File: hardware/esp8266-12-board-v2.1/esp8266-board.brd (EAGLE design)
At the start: 35.4 x 38 mm, 26 parts, among them T1 AMS1117, T2 LM7805

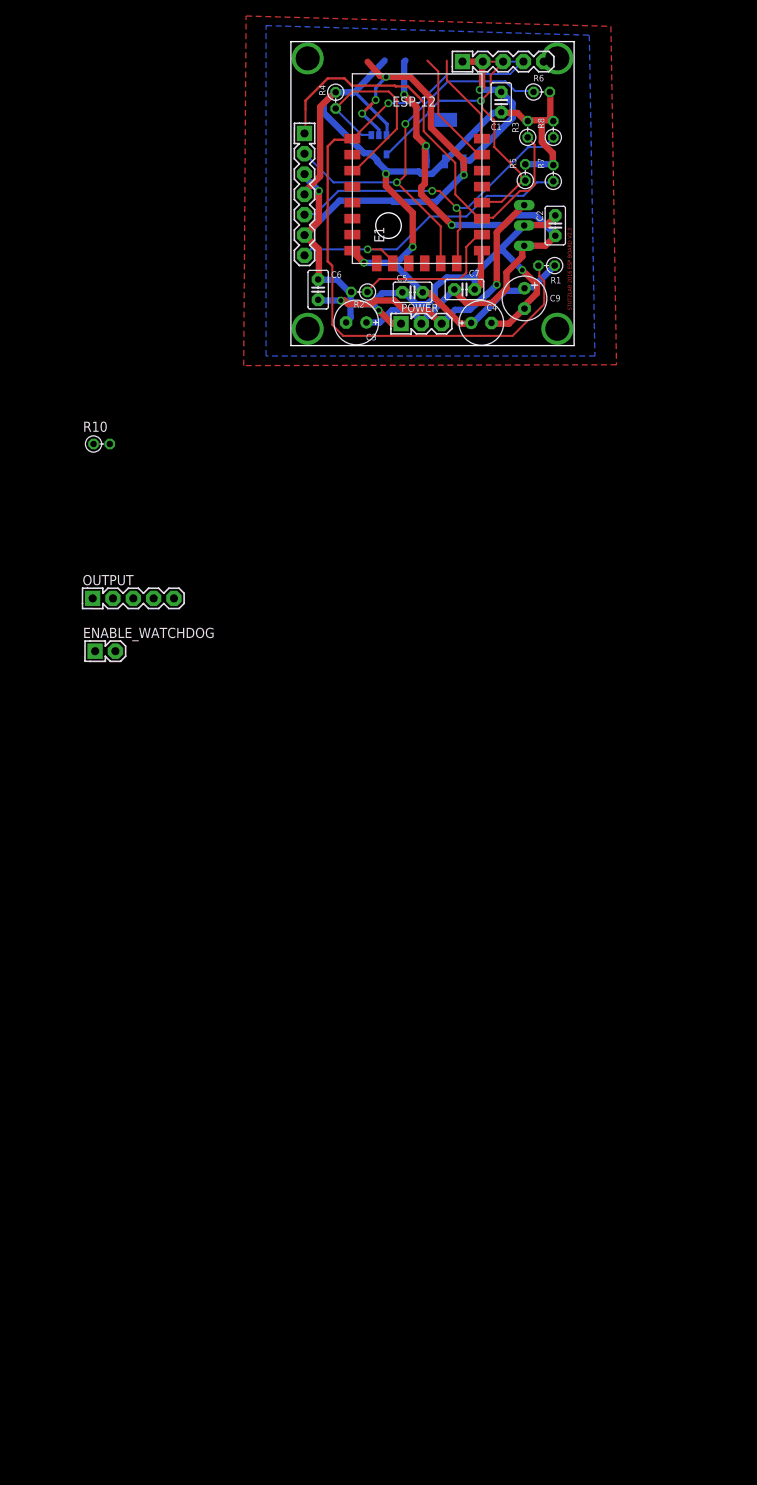
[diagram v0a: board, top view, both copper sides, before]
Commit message: Added watchdog from maxim
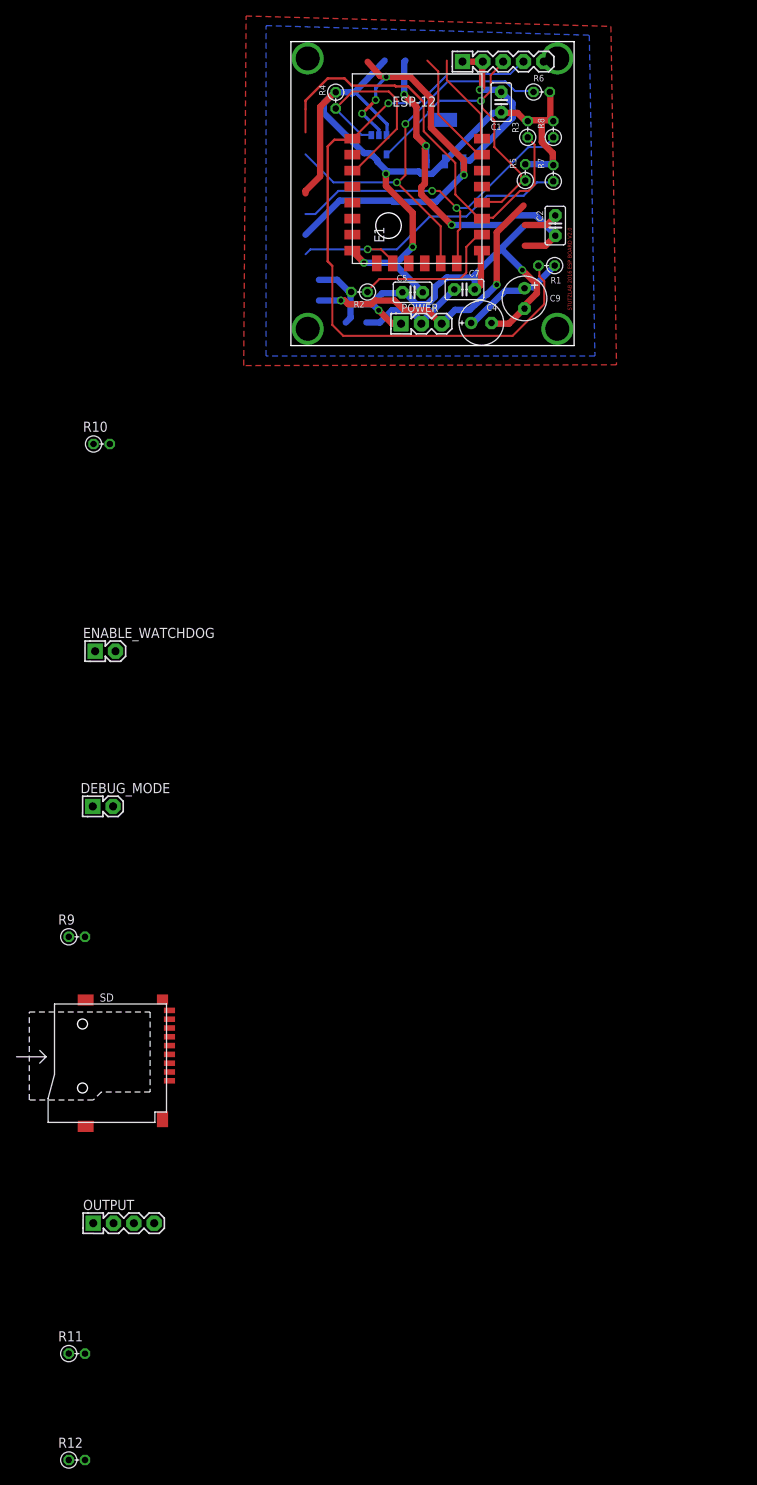
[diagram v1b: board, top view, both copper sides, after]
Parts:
- removed C3: 470uF, rcl:E2,5-6E
- removed C6: 0.22uF, capacitor-wima:C2.5-2
- removed SD1: CS SI GND 3.3V SCK GND SO, stutz-eagle:PIN-HEADER-7PIN
- removed T2: LM7805, stutz-components-library:TO-220
- added DEBUG_MODE: PIN-HEADER-2PIN, stutz-components-library:PIN-HEADER-2PIN
- added R11, R12: 500, stutz-components-library:RESISTOR-V1
- added R9: 10k, stutz-components-library:RESISTOR-V1
- added SD: MICROSD-TRANSFLASH, stutz-components-library:MICROSD-TRANSFLASH
- OUTPUT: value PIN-HEADER-5PIN -> PIN-HEADER-4PIN; device stutz-components-library:PIN-HEADER-5PIN -> stutz-components-library:PIN-HEADER-4PIN
- POWER: value GND +5V <35V -> GND +5V +3.3V
- W1: value TPS3823-33 -> MAX6373KA+T
- moved OUTPUT 78.1 mm to (-20.9, -109.7)
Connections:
- removed net +24V: C6.1, POWER.3, T2.INPUT
- new net N$6: C5.2
- new net N$7: FIRMWARE.2, R11.2
- new net N$8: FIRMWARE.3, R12.2
- net +3.3V: now also C7.1, DEBUG_MODE.1, POWER.3, SD.6; no longer OUTPUT.2, SD1.4
- net +5V: no longer C3.+, C7.1, OUTPUT.3, T2.OUTPUT
- net ESP_GPIO0: now also R11.1; no longer FIRMWARE.2
- net ESP_GPIO12: now also SD.7; no longer SD1.7
- net ESP_GPIO13: now also SD.3; no longer SD1.2
- net ESP_GPIO14: now also SD.5; no longer SD1.5
- net ESP_GPIO4: now also SD.2; no longer SD1.1
- net ESP_GPIO5: now also DEBUG_MODE.2, R9.2
- net ESP_RST: now also R12.1; no longer FIRMWARE.3
- net ESP_RX: no longer OUTPUT.4
- net ESP_TX: no longer OUTPUT.5
- net GND: now also R9.1, SD.4, SD.S1, SD.S2, SD.S3, SD.S4; no longer C3.-, C5.2, C6.2, OUTPUT.1, SD1.3, SD1.6, T2.GND
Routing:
- net +24V: track 37.4 -> 0.00 mm, vias 2 -> 0
- net +3.3V: track 128.2 -> 157.1 mm, vias 3 -> 5
- net GND: track 160.2 -> 143.3 mm, vias 8 -> 7
- net +5V: track 73.3 -> 58.6 mm
- net ESP_GPIO0: track 42.7 -> 40.0 mm
- net ESP_RST: track 87.5 -> 85.1 mm

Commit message: Updating board for SMD usage
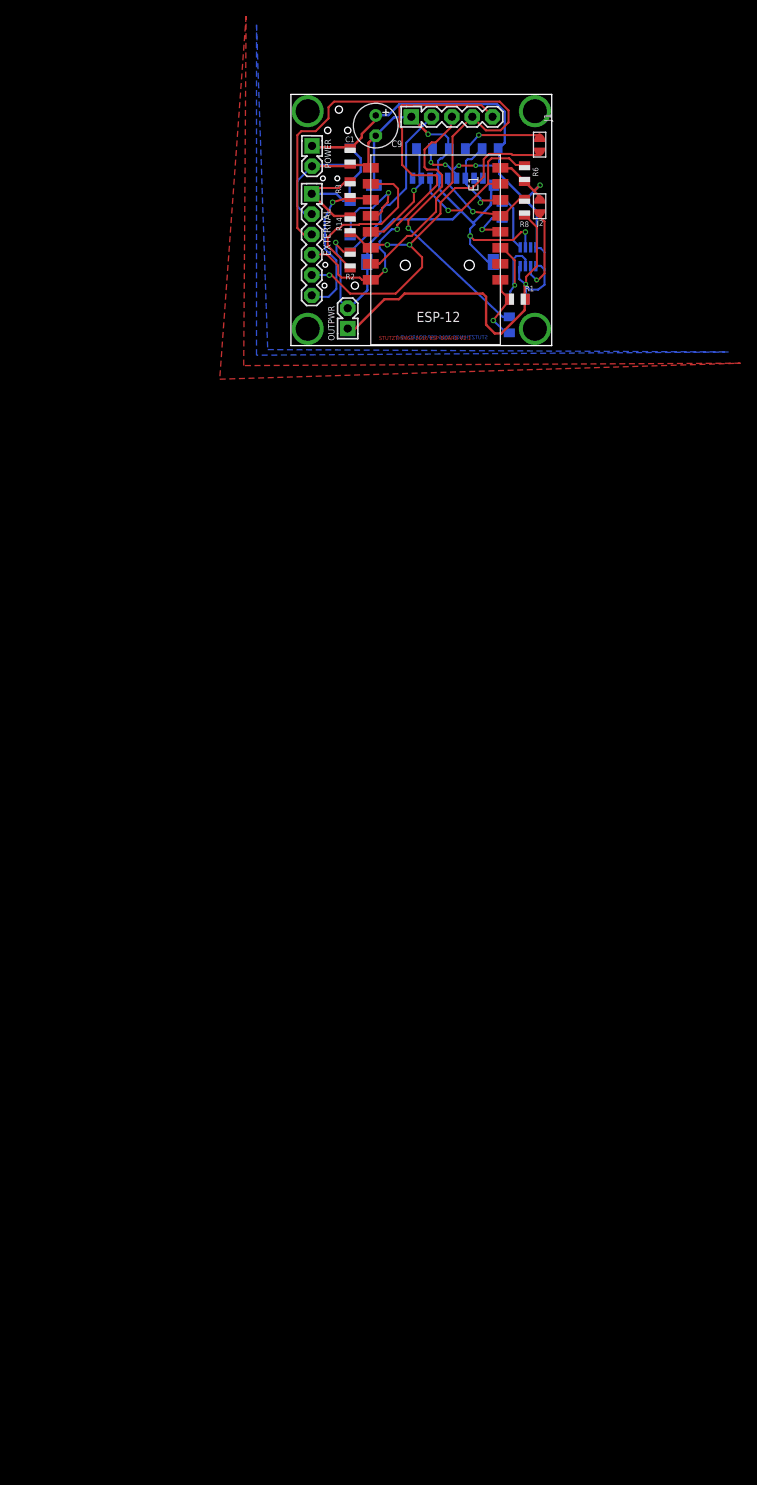
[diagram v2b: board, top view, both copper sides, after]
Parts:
- removed C2, C5: 10uF, capacitor-wima:C2.5-2
- removed C4: 470uF, rcl:E2,5-6E
- removed C7: 0.1uF, capacitor-wima:C2.5-2
- removed DEBUG_MODE, ENABLE_WATCHDOG: PIN-HEADER-2PIN, stutz-components-library:PIN-HEADER-2PIN
- removed FIRMWARE: GND DTR RTS RX TX, stutz-components-library:PIN-HEADER-5PIN
- removed OUTPUT: PIN-HEADER-4PIN, stutz-components-library:PIN-HEADER-4PIN
- removed T1: AMS1117, stutz-eagle:SOT-223
- added C3: 1uF, stutz-components-library:SMD0805
- added EXTERNAL: IO2 IO5 TX RX GND +3.3V, stutz-components-library:PIN-HEADER-6PIN
- added J1: DEBUG, stutz-components-library:JUMPER-PAD-2-ROUND
- added J2: WATCHDOG, stutz-components-library:JUMPER-PAD-2-ROUND
- added OUTPWR: +3.3V GND, stutz-components-library:PIN-HEADER-2PIN
- added P3: GND DTR RTS RX TX, stutz-components-library:PIN-HEADER-5PIN
- added R13: 350, stutz-components-library:SMD0805
- added R14: 3.3k, stutz-components-library:SMD0805
- C1: device capacitor-wima:C2.5-2 -> stutz-components-library:SMD0805
- E1: value ESP8266-12 -> ESP8266-12-2; device stutz-eagle:ESP8266-12 -> stutz-components-library:ESP8266-12-2
- POWER: value GND +5V +3.3V -> GND +3.3V; device stutz-eagle:PIN-HEADER-3PIN -> stutz-components-library:PIN-HEADER-2PIN
- R1, R10, R2, R3, R4, R5, R6, R7, R8: value 10k -> 3.3k; device stutz-components-library:RESISTOR-V1 -> stutz-components-library:SMD0805
- R11, R12: value 500 -> 350; device stutz-components-library:RESISTOR-V1 -> stutz-components-library:SMD0805
- R9: value 10k -> 350; device stutz-components-library:RESISTOR-V1 -> stutz-components-library:SMD0805
- W1: value MAX6373KA+T -> MAX6369KA+T; device stutz-components-library:SOT23-5/TSOT25 -> stutz-components-library:SOT23-8
- moved R12 151.8 mm to (27.3, 2.60), flipped to the bottom, turned to 90 degrees
- moved R11 142.8 mm to (7.40, 12.7), flipped to the bottom, turned to 270 degrees
- moved SD 110.5 mm to (10.0, 5.70), flipped to the bottom, turned to 90 degrees
- moved R9 109.3 mm to (20.8, 24.6), flipped to the bottom, turned to 180 degrees
- moved R10 54.5 mm to (16.7, 24.6), flipped to the bottom, turned to 180 degrees
- moved R4 33.5 mm to (28.3, 5.80), flipped to the bottom, turned to 0 degrees
- moved C9 28.5 mm to (10.6, 27.5)
- moved POWER 25.0 mm to (2.64, 23.7), turned to 270 degrees
- moved R3 23.5 mm to (7.40, 19.5)
- moved W1 23.3 mm to (29.6, 11.2)
- moved R5 22.4 mm to (7.40, 17.0), flipped to the bottom
- moved C1 20.1 mm to (7.41, 23.7), turned to 270 degrees
- moved R8 10.6 mm to (29.2, 17.3), turned to 270 degrees
- moved R6 10.5 mm to (29.2, 21.5), turned to 270 degrees
- moved E1 8.38 mm to (17.8, 13.3)
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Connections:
- removed net +5V: C2.1, POWER.2, T1.3
- new net N$10: R13.2, W1.1
- net +3.3V: now also C3.1, EXTERNAL.1, J2.2, OUTPWR.1, POWER.1, R14.2, W1.4, W1.8; no longer C4.+, C5.1, C7.1, DEBUG_MODE.1, POWER.3, T1.2, W1.3
- net ESP_CH_PD: now also W1.7; no longer W1.1
- net ESP_GPIO16: now also R13.1; no longer ENABLE_WATCHDOG.1
- net ESP_GPIO2: now also EXTERNAL.6
- net ESP_GPIO5: now also EXTERNAL.5, J1.1, R14.1; no longer DEBUG_MODE.2, R9.2
- net ESP_RX: now also EXTERNAL.3, P3.4; no longer FIRMWARE.4
- net ESP_TX: now also EXTERNAL.4, P3.5; no longer FIRMWARE.5
- net GND: now also C3.2, EXTERNAL.2, OUTPWR.2, P3.1, POWER.2; no longer C2.2, C4.-, C7.2, FIRMWARE.1, POWER.1, T1.1
- net N$1: now also J2.1, W1.6; no longer ENABLE_WATCHDOG.2, W1.4
- net N$6: now also J1.2, R9.2; no longer C5.2
- net N$7: now also P3.2; no longer FIRMWARE.2
- net N$8: now also P3.3; no longer FIRMWARE.3
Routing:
- net ESP_RST: track 85.1 -> 8.90 mm
- net ESP_RX: track 14.8 -> 75.0 mm
- net +5V: track 58.6 -> 0.00 mm, vias 3 -> 0
- net ESP_GPIO5: track 0.00 -> 51.3 mm, vias 0 -> 3
- net ESP_TX: track 11.6 -> 51.7 mm, vias 0 -> 2
- net N$8: track 0.00 -> 36.1 mm, vias 0 -> 1
- net ESP_GPIO2: track 53.5 -> 20.3 mm, vias 0 -> 1
- net ESP_GPIO13: track 51.8 -> 20.7 mm, vias 2 -> 1
- net ESP_GPIO14: track 43.9 -> 12.8 mm, vias 2 -> 1
- net GND: track 143.3 -> 112.4 mm, vias 7 -> 4
- net ESP_GPIO0: track 40.0 -> 13.1 mm
- net ESP_GPIO12: track 38.7 -> 11.8 mm
- net N$7: track 0.00 -> 21.4 mm
- net ESP_GPIO4: track 0.00 -> 14.2 mm, vias 0 -> 1
- net ESP_CH_PD: track 26.2 -> 13.7 mm, vias 0 -> 1
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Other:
- board size 35.4 x 38 mm -> 32.6 x 31.4 mm
- board text added: "STUTZTHINGS 2016 ESP BOARD V2.1"
- board text removed: "STUTZLAB 2016 ESP BOARD V2.0"
- board text removed: "TODO: - RETIRAR VIAS DE BAIXO DO REGULADOR DE TENSAO - EXPOR ANTENA WIFI PARA FORA DA PLACA - AUMENTAR TAMANHO BURACO DO POWER - REVISAR LOGICA DO BOOTSTRAP"

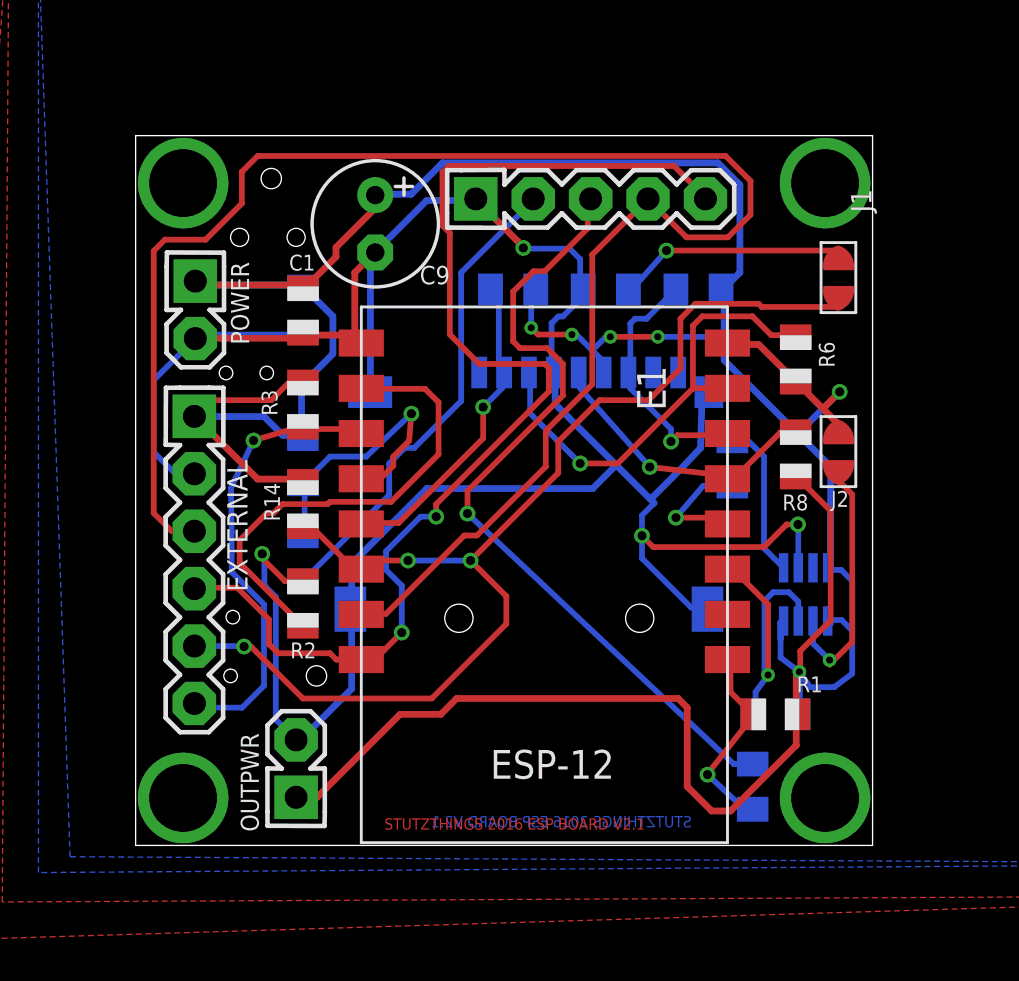
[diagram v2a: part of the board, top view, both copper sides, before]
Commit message: PCB revision to v2.1
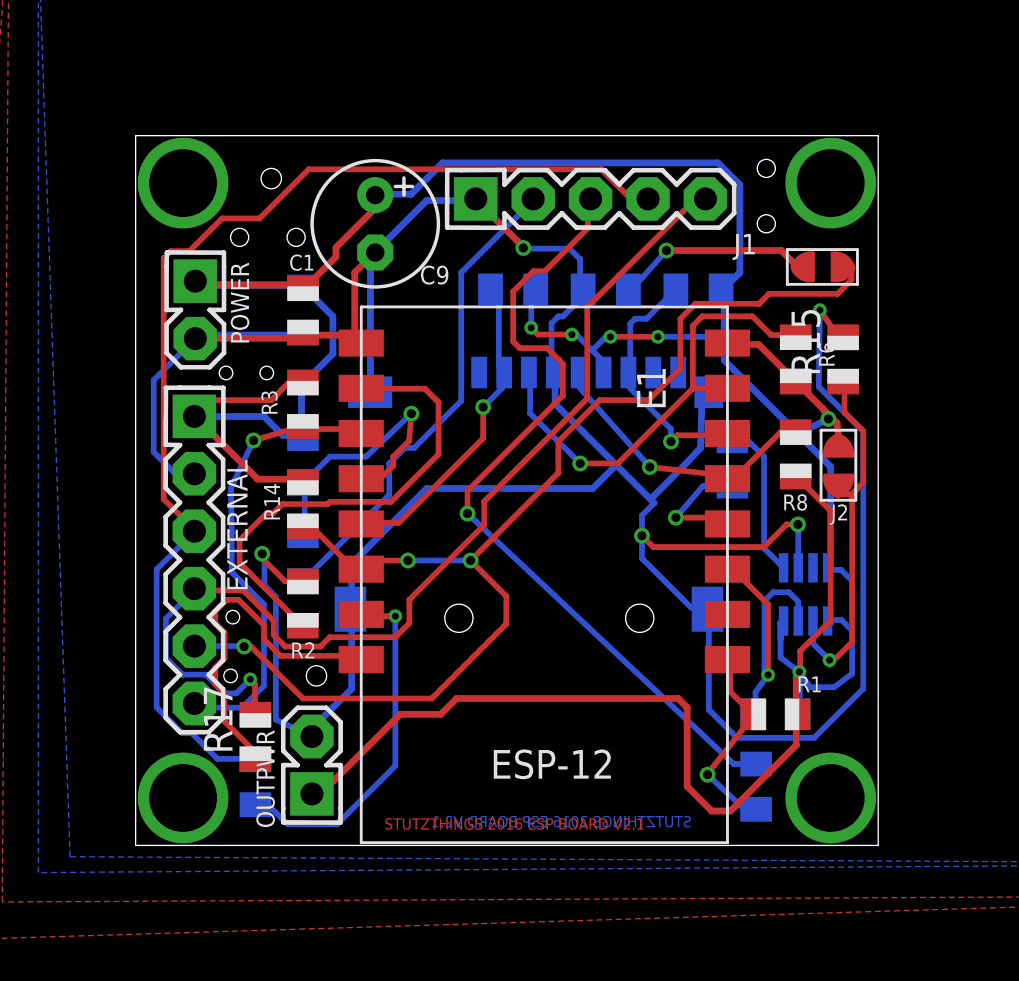
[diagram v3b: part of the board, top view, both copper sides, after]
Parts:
- added R15: 3.3k, stutz-components-library:SMD0805
- added R16, R17: 350, stutz-components-library:SMD0805
- moved J1 0.86 mm to (30.4, 25.6), turned to 180 degrees
- moved OUTPWR 0.72 mm to (7.80, 3.55)
- moved J2 0.60 mm to (31.1, 16.8)
- moved R12 0.15 mm to (27.4, 2.60)
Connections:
- new net RX_PROT: EXTERNAL.3, P3.4, R16.2
- new net TX_PROT: EXTERNAL.4, P3.5, R17.2
- net ESP_RX: now also R16.1; no longer EXTERNAL.3, P3.4
- net ESP_TX: now also R17.1; no longer EXTERNAL.4, P3.5
- net GND: now also R15.2
- net N$1: now also R15.1
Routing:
- net ESP_RX: track 75.0 -> 15.8 mm, vias 0 -> 1
- net RX_PROT: track 0.00 -> 50.1 mm
- net TX_PROT: track 0.00 -> 45.7 mm, vias 0 -> 1
- net ESP_TX: track 51.7 -> 15.8 mm, vias 2 -> 0
- net GND: track 112.4 -> 145.3 mm, vias 4 -> 5
- net N$1: track 11.0 -> 16.3 mm
- net N$6: track 10.8 -> 9.26 mm
- net ESP_GPIO5: track 51.3 -> 52.7 mm
- net +3.3V: track 156.4 -> 155.2 mm
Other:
- board size 32.6 x 31.4 mm -> 32.9 x 31.4 mm
